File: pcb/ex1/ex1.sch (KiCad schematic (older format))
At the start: 33 parts, among them J1 USB_B, J2 Conn_01x06, J3 Conn_01x08, J4 Conn_01x10, J5 Conn_01x08, J6 Conn_01x08, J7 Conn_01x08, J8 Conn_02x05_Counter_Clockwise, SW1 SW_DIP_x01, U1 AMS1117-3.3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

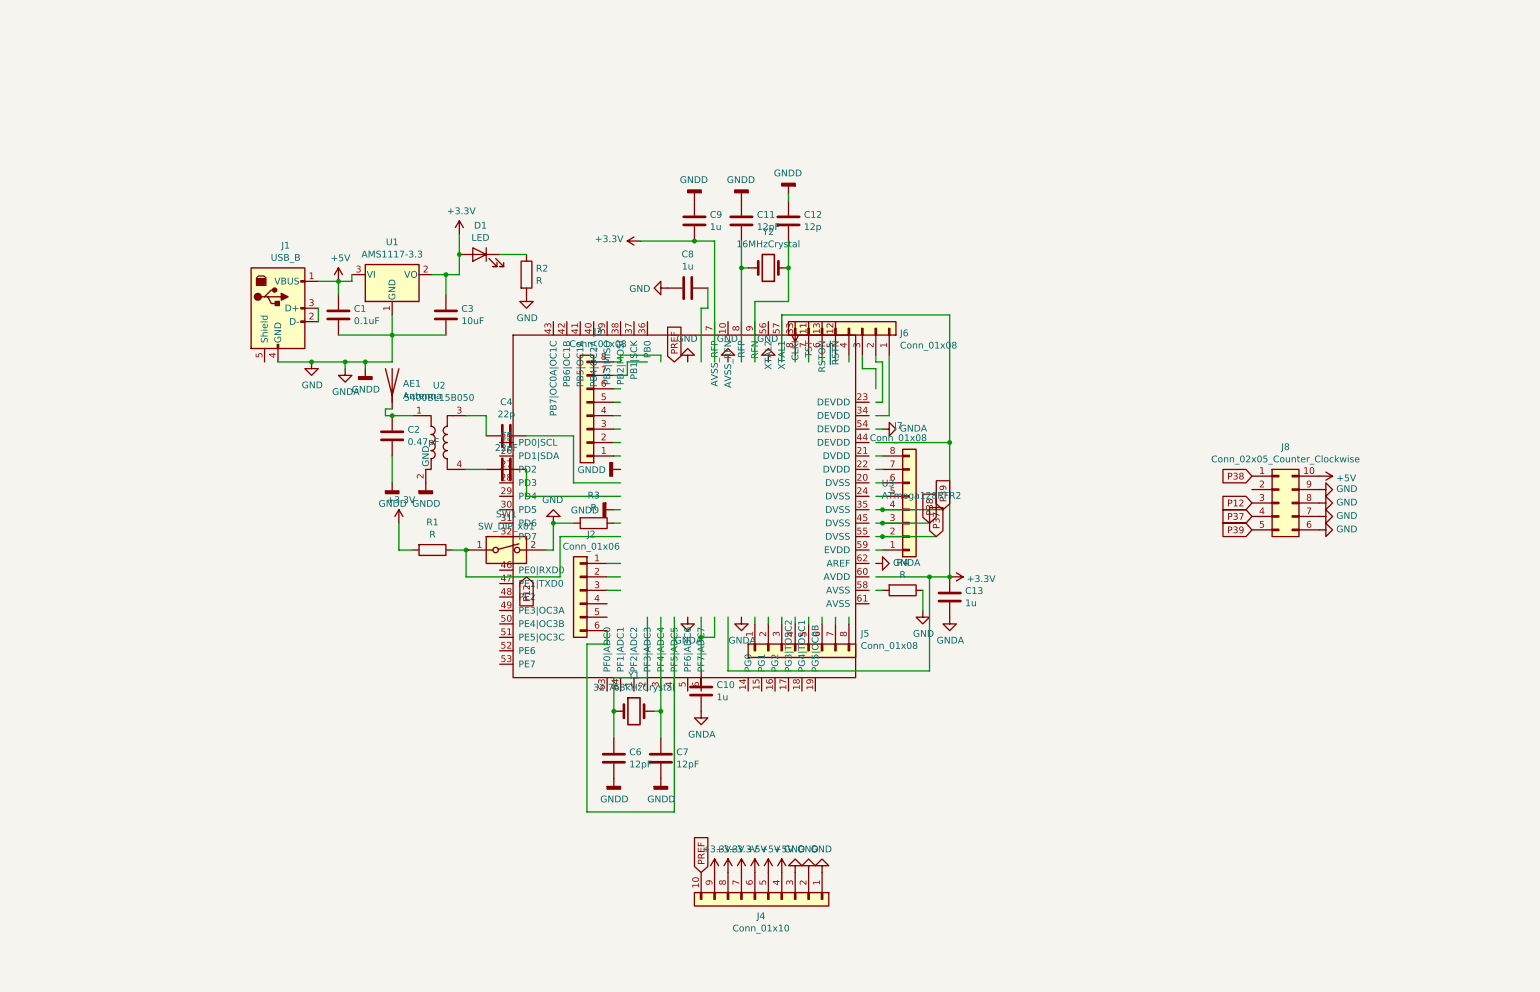
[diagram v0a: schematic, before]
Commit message: Changed schematic
for better comprehension on the schematic
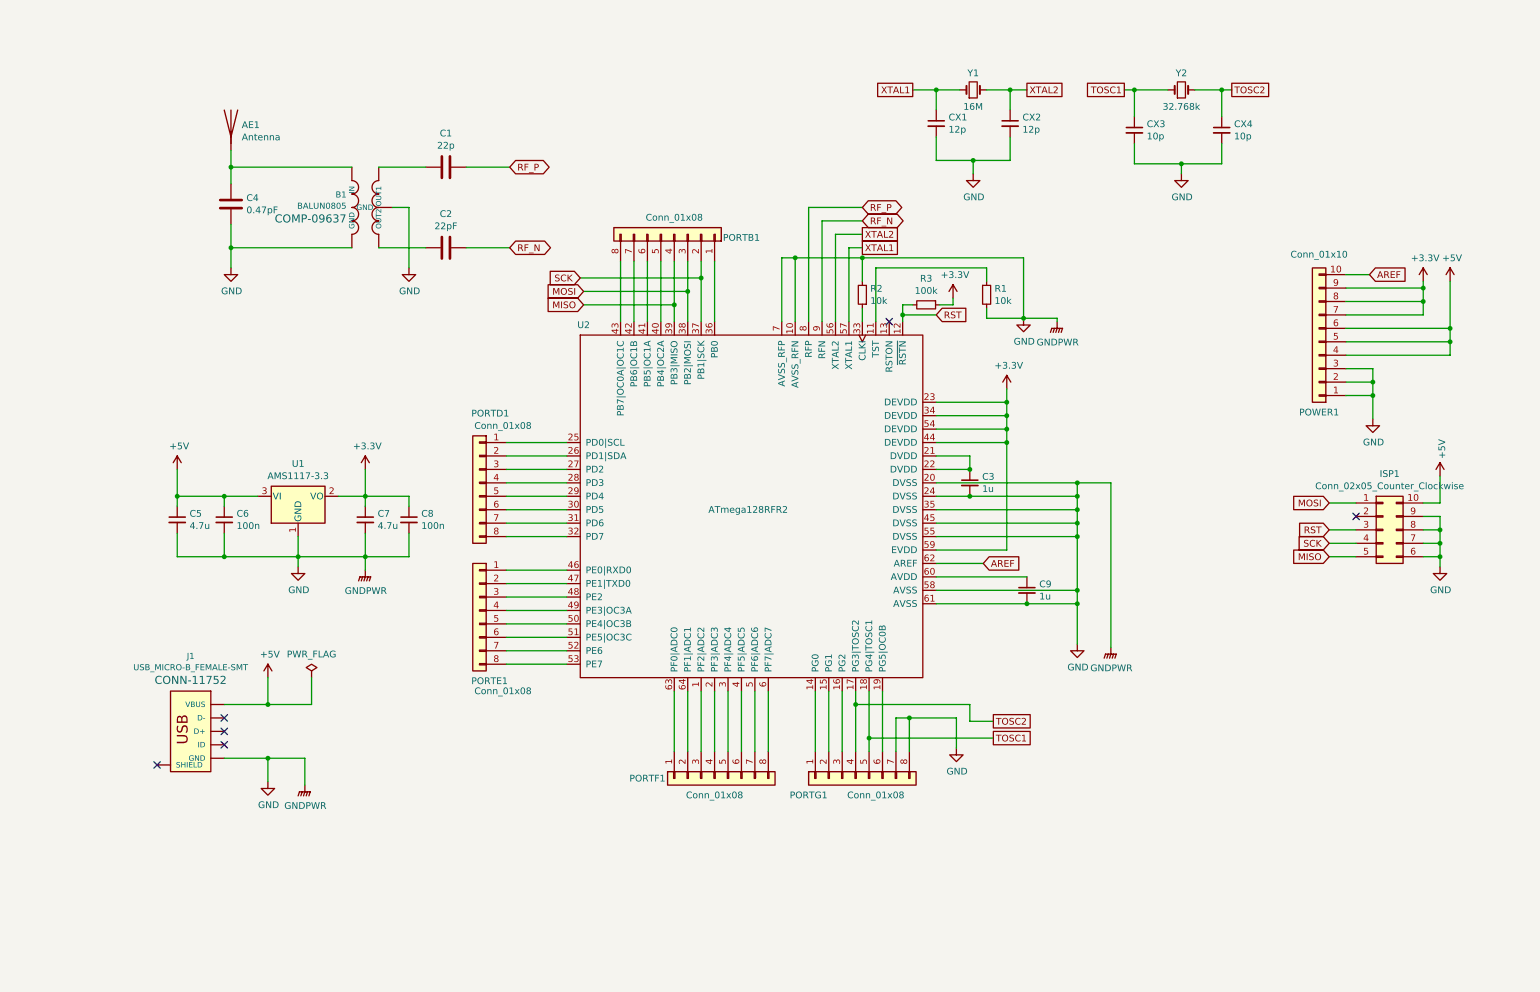
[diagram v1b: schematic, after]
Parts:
- removed C1: 0.1uF, symbol Device:C
- removed C10, C13, C8, C9: 1u, symbol Device:C
- removed C11, C6, C7: 12pF, symbol Device:C
- removed C12: 12p, symbol Device:C
- removed C3: 10uF, symbol Device:C
- removed D1: LED, symbol Device:LED
- removed J1: USB_B, symbol Connector:USB_B
- removed J2: Conn_01x06, symbol Connector_Generic:Conn_01x06
- removed J3, J5, J6, J7: Conn_01x08, symbol Connector_Generic:Conn_01x08
- removed R1, R2, R3, R4: R, symbol Device:R
- removed SW1: SW_DIP_x01, symbol Switch:SW_DIP_x01
- removed U2: 5400BL15B050, RF_Converter:Balun_Johanson_5400BL15B050E, symbol Transformer:5400BL15B050
- removed U3: ATmega128RFR2, symbol RFR2_lib:ATmega128RFR2
- removed Y1: 32.768kHzCrystal, symbol Device:Crystal
- removed Y2: 16MHzCrystal, symbol Device:Crystal
- added B1: BALUN0805, BALUN-0805, symbol SparkFun-RF:BALUN0805
- added C3, C9: 1u, symbol Device:C_Small
- added C5, C7: 4.7u, symbol Device:C_Small
- added C6, C8: 100n, symbol Device:C_Small
- added CX1, CX2: 12p, symbol Device:C_Small
- added CX3, CX4: 10p, symbol Device:C_Small
- added J1: USB_MICRO-B_FEMALE-SMT, USB-B-MICRO-SMD, symbol SparkFun-Connectors:USB_MICRO-B_FEMALE-SMT
- added PORTB1, PORTD1, PORTE1, PORTF1, PORTG1: Conn_01x08, symbol Connector_Generic:Conn_01x08
- added R1, R2: 10k, symbol Device:R_Small
- added R3: 100k, symbol Device:R_Small
- added U2: ATmega128RFR2, symbol RFR2_lib:ATmega128RFR2
- added Y1: 16M, symbol Device:Crystal_Small
- added Y2: 32.768k, symbol Device:Crystal_Small
- renumbered C4 to C1, C5 to C2, C2 to C4, J8 to ISP1, J4 to POWER1
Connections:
- net labels added: AREF, GNDPWR, MISO, MOSI, RF_N, RF_P, RST, SCK, TOSC1, TOSC2, XTAL1, XTAL2
- net labels removed: GNDA, GNDD, P12, P37, P38, P39, PREF
- wire segments 138 -> 213
- no-connect marks 0 -> 6
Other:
- moved on the sheet: AE1, C1, C2, C4, ISP1, POWER1

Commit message: Refined design for antenna
Added tuning inductors for impedance matching
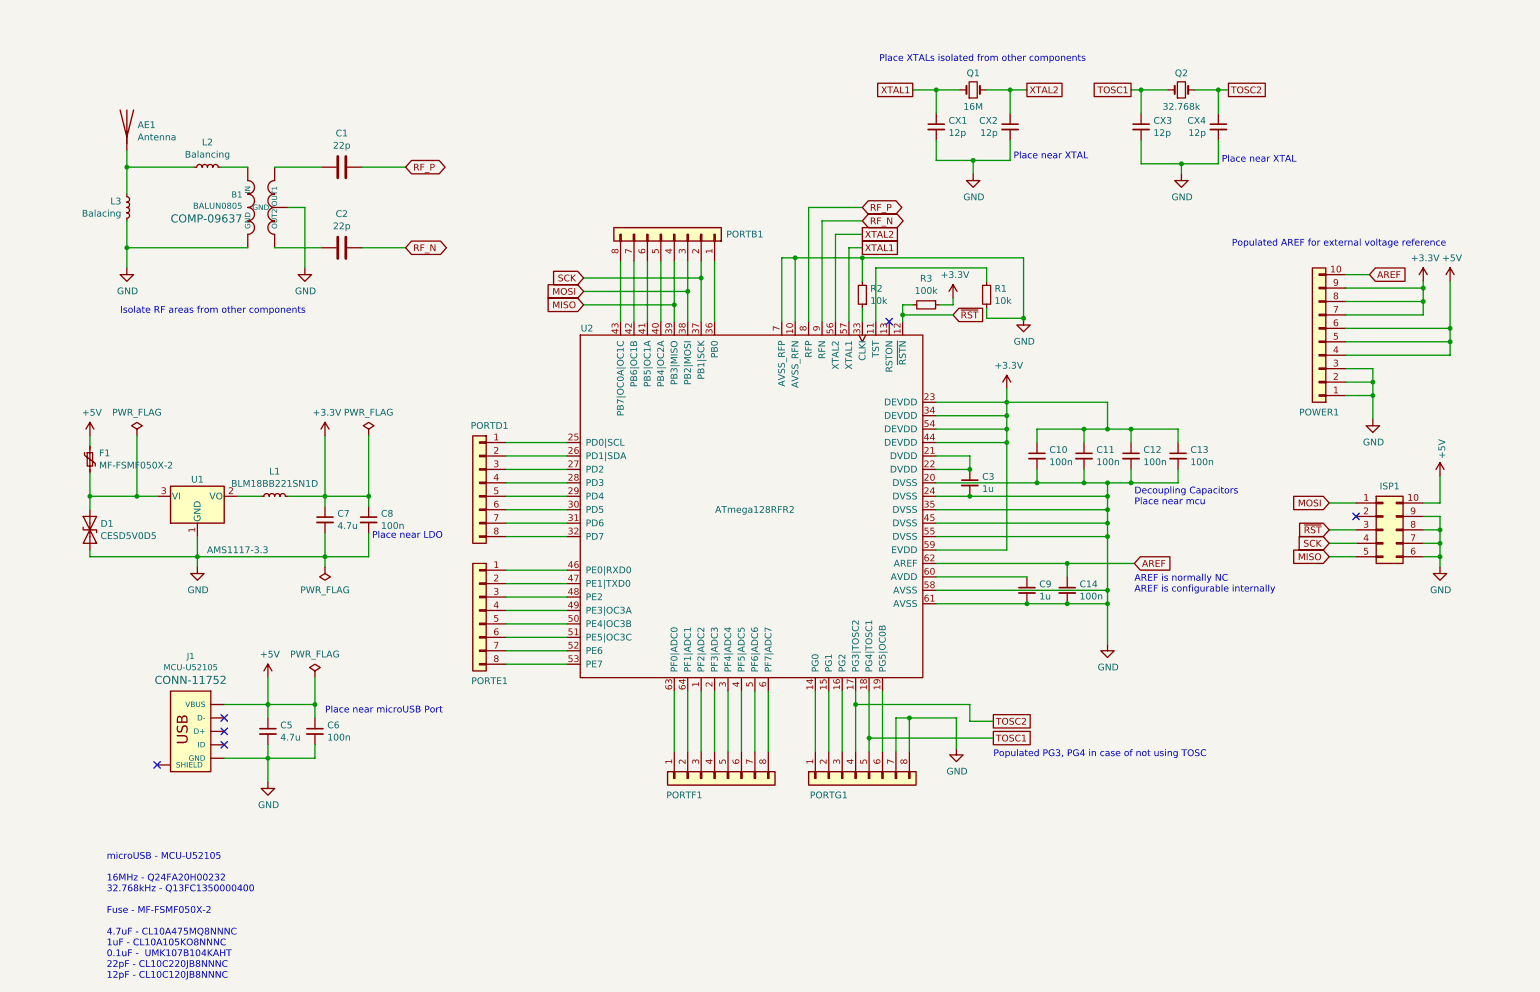
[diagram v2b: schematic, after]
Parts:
- removed C4: 0.47pF, symbol Device:C
- added C10, C11, C12, C13, C14: 100n, Capacitor_SMD:C_0603_1608Metric_Pad1.05x0.95mm_HandSolder, symbol Device:C_Small
- added D1: CESD5V0D5, Diode_SMD:D_SOD-523, symbol Device:D_TVS
- added F1: MF-FSMF050X-2, Fuse:Fuse_0603_1608Metric_Pad1.05x0.95mm_HandSolder, symbol Device:Polyfuse_Small
- added L1: BLM18BB221SN1D, Inductor_SMD:L_0603_1608Metric_Pad1.05x0.95mm_HandSolder, symbol Device:L_Small
- added L2: Balancing, Inductor_SMD:L_0603_1608Metric_Pad1.05x0.95mm_HandSolder, symbol Device:L_Small
- added L3: Balacing, Inductor_SMD:L_0603_1608Metric_Pad1.05x0.95mm_HandSolder, symbol Device:L_Small
- AE1: footprint (none) -> RF:ANT-2.4GHZ-6.5X2.2MM
- B1: footprint BALUN-0805 -> RF:BALUN-0805
- C1, C3, C5, C6, C7, C8, C9, CX1, CX2: footprint (none) -> Capacitor_SMD:C_0603_1608Metric_Pad1.05x0.95mm_HandSolder
- C2: value 22pF -> 22p; footprint (none) -> Capacitor_SMD:C_0603_1608Metric_Pad1.05x0.95mm_HandSolder
- CX3, CX4: value 10p -> 12p; footprint (none) -> Capacitor_SMD:C_0603_1608Metric_Pad1.05x0.95mm_HandSolder
- ISP1: footprint (none) -> Connector_PinSocket_2.54mm:PinSocket_2x05_P2.54mm_Vertical
- J1: value USB_MICRO-B_FEMALE-SMT -> MCU-U52105; footprint USB-B-MICRO-SMD -> ESP8266:MCU-U52105
- PORTB1, PORTD1, PORTE1, PORTF1, PORTG1: footprint (none) -> Connector_PinSocket_2.54mm:PinSocket_1x08_P2.54mm_Vertical
- POWER1: footprint (none) -> Connector_PinSocket_2.54mm:PinSocket_1x10_P2.54mm_Vertical
- Q1: renamed from Y1; footprint (none) -> Crystal:Crystal_SMD_2520-4Pin_2.5x2.0mm
- Q2: renamed from Y2; footprint (none) -> Crystal:Crystal_SMD_EuroQuartz_EQ161-2Pin_3.2x1.5mm_HandSoldering
- R1, R2, R3: footprint (none) -> Resistor_SMD:R_0805_2012Metric_Pad1.15x1.40mm_HandSolder
- U2: footprint (none) -> Package_DFN_QFN:QFN-64-1EP_9x9mm_P0.5mm_EP4.7x4.7mm_ThermalVias
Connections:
- net +3V3: now also C10.1, C11.1, C12.1, C13.1, L1.2; no longer U1.2 (VO)
- net +5V: now also F1.1; no longer U1.3 (VI)
- net AREF: now also C14.1
- net GND: now also C10.2, C11.2, C12.2, C13.2, C14.2, D1.2 (A2), L3.1
- net at AE1.1 (A): now also L2.1, L3.2; no longer B1.1 (IN)
- net RST renamed ~RST
- new net: B1.1 (IN), L2.2
- new net: L1.1, U1.2 (VO)
- new net: D1.1 (A1), F1.2, U1.3 (VI)
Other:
- note added: "AREF is normally NC\nAREF is configurable internally"
- note added: "Decoupling Capacitors\nPlace near mcu"
- note added: "Isolate RF areas from other components"
- note added: "Place XTALs isolated from other components"
- note added: "Place near LDO"
- note added: "Place near XTAL"
- note added: "Place near microUSB Port"
- note added: "Populated AREF for external voltage reference"
- note added: "Populated PG3, PG4 in case of not using TOSC"
- note added: "microUSB - MCU-U52105\n\n16MHz - Q24FA20H00232\n32.768kHz - Q13FC1350000400\n\nFuse - MF-FSMF050X-2\n\n4.7uF - CL10A475MQ8NNNC\n1uF - CL10A105KO8NNNC\n0.1uF - UMK107B104KAHT\n22pF - CL10C220JB8NNNC\n12pF - CL10C120JB8NNNC"
- moved on the sheet: AE1, B1, C1, C2, C5, C6, C7, C8, CX1, CX2, CX3, CX4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

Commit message: Finished schematic design
Connected all the schematic symbols to matching footprints.

Also I made a reference layout of the board.
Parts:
- removed AE1: Antenna, RF:ANT-2.4GHZ-6.5X2.2MM, symbol Device:Antenna
- removed B1: BALUN0805, RF:BALUN-0805, symbol SparkFun-RF:BALUN0805
- removed J1: MCU-U52105, ESP8266:MCU-U52105, symbol SparkFun-Connectors:USB_MICRO-B_FEMALE-SMT
- removed Q1: 16M, Crystal:Crystal_SMD_2520-4Pin_2.5x2.0mm, symbol Device:Crystal_Small
- added AE1: 2450AT42B100E, RFR2:2450AT42B100E, symbol RFR2_lib:2450AT42B100E
- added B1: 2450BM15A0015E, RFR2:BALUN-0805, symbol RFR2_lib:BALUN0805
- added J1: USB_MICRO-B_FEMALE-SMT, RFR2:MCU-U52105, symbol RFR2_lib:USB_MICRO-B_FEMALE-SMT
- added Q1: 16M, Crystal:Crystal_SMD_2520-4Pin_2.5x2.0mm, symbol Device:Crystal_GND24_Small
- added SW1: TS342A2P, RFR2:TS342A2P, symbol Switch:SW_SPST
- L3: value Balacing -> Balancing
- R1, R2, R3: footprint Resistor_SMD:R_0805_2012Metric_Pad1.15x1.40mm_HandSolder -> Resistor_SMD:R_0603_1608Metric_Pad1.05x0.95mm_HandSolder
- U2: footprint Package_DFN_QFN:QFN-64-1EP_9x9mm_P0.5mm_EP4.7x4.7mm_ThermalVias -> Package_DFN_QFN:QFN-64-1EP_9x9mm_P0.5mm_EP4.7x4.7mm
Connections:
- net labels added: +VDC
- wire segments 235 -> 245
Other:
- note added: "microUSB - MCU-U52105\n\n16MHz - Q24FA20H00232\n32.768kHz - Q13FC1350000400\n\nFuse - MF-FSMF050X-2\n\n4.7uF - CL10A475MQ8NNNC\n1uF - CL10A105KO8NNNC\n0.1uF - UMK107B104KAHT\n22pF - CL10C220JB8NNNC\n12pF - CL10C120JB8NNNC\n\n100k - RMC16K104FTP\n10k - RMC16K103FTP"
- note removed: "microUSB - MCU-U52105\n\n16MHz - Q24FA20H00232\n32.768kHz - Q13FC1350000400\n\nFuse - MF-FSMF050X-2\n\n4.7uF - CL10A475MQ8NNNC\n1uF - CL10A105KO8NNNC\n0.1uF - UMK107B104KAHT\n22pF - CL10C220JB8NNNC\n12pF - CL10C120JB8NNNC"
- moved on the sheet: C5, C6, D1, F1
